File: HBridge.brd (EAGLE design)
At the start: 59.7 x 53.3 mm, 42 parts, among them IC1 74HC08D, IC2 A4954, J1 In 3/4, J2 Power, J3 In 1/2, J4 Output A, J5 Output B, J6 Digital_8_13, J7 Analog, J8 Digital_0_7

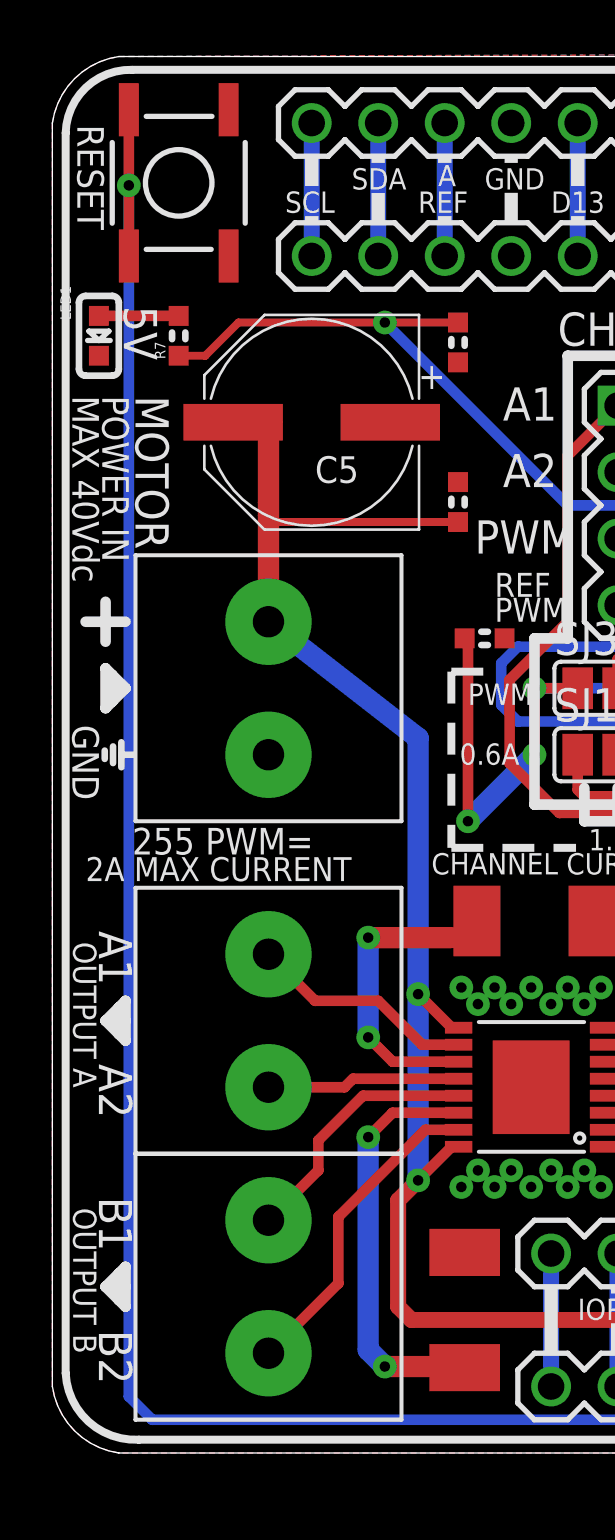
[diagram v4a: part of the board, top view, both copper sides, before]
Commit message: Replaced reset button with smaller 2-pin version
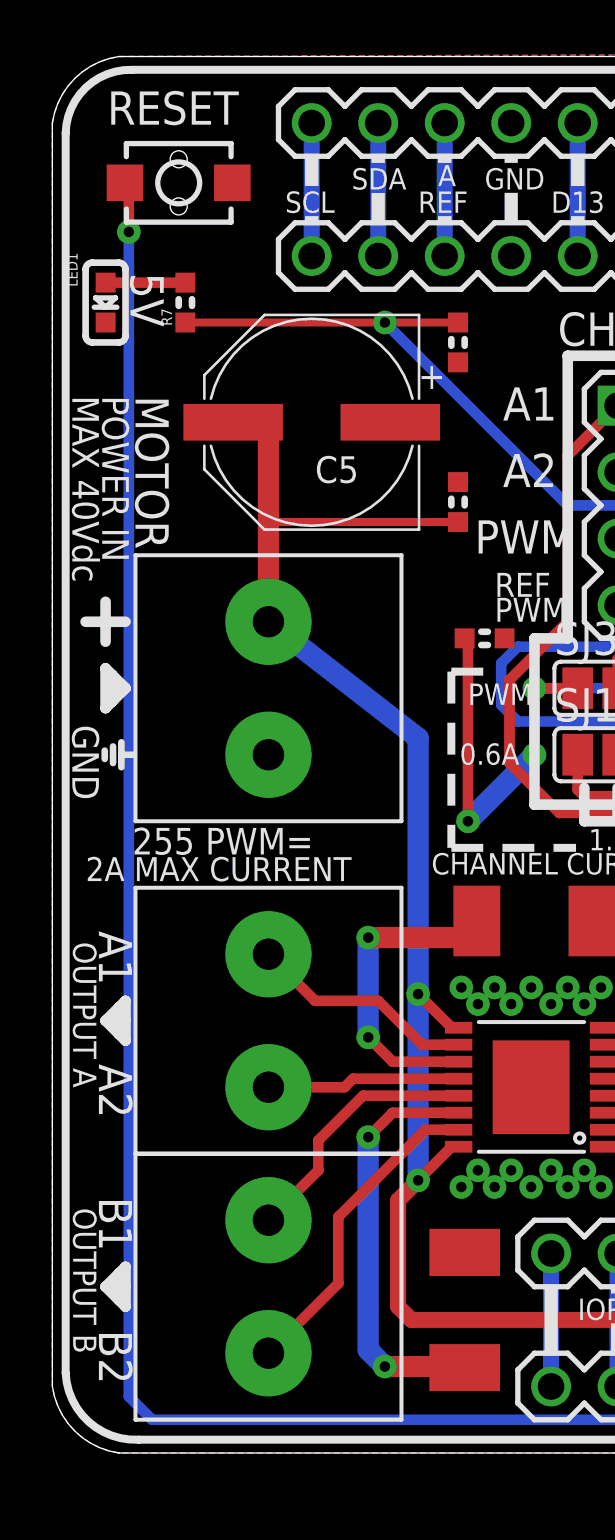
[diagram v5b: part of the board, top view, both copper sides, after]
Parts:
- S1: device freetronics:TACTILE_SWITCH_SMD -> freetronics-master-v1:TACTILE_SWITCH_SMD_2PIN_TINY
- moved R7 1.30 mm to (5.08, 43.9)
- moved LED1 1.30 mm to (2.03, 43.9)
- turned S1 to 0 degrees
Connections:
- net GND: no longer S1.1
- net RESET: now also S1.1; no longer S1.3, S1.4
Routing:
- net RESET: track 136.2 -> 130.8 mm
- net +5V: track 193.4 -> 192.6 mm
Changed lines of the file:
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@@
 <wire x1="28.09875" y1="27.78125" x2="28.09875" y2="27.305" width="0.3048" layer="21"/>
 <wire x1="28.09875" y1="27.305" x2="27.6225" y2="27.305" width="0.3048" layer="21"/>
-<text x="0.9525" y="50.7365" size="1.016" layer="21" ratio="15" rot="SR270">RESET</text>
-<text x="2.7305" y="43.815" size="1.27" layer="21" ratio="15" rot="SR270">5V</text>
+<text x="2.0955" y="50.7365" size="1.27" layer="21" ratio="15" rot="SR0">RESET</text>
+<text x="2.9845" y="45.085" size="1.27" layer="21" ratio="15" rot="SR270">5V</text>
 <text x="13.97" y="40.64" size="1.016" layer="21" ratio="15">+</text>
 <text x="1.778" y="19.939" size="1.27" layer="21" ratio="15" rot="SR270">A1</text>
@@
 <text x="26.9875" y="42.037" size="1.9304" layer="21" ratio="15">~</text>
 <text x="24.4475" y="42.037" size="1.9304" layer="21" ratio="15">~</text>
-<wire x1="2.286" y1="44.196" x2="1.27" y2="44.196" width="0.254" layer="21"/>
-<wire x1="1.27" y1="44.196" x2="1.016" y2="43.942" width="0.254" layer="21" curve="90"/>
-<wire x1="1.016" y1="43.942" x2="1.016" y2="41.402" width="0.254" layer="21"/>
-<wire x1="1.016" y1="41.402" x2="1.27" y2="41.148" width="0.254" layer="21" curve="90"/>
-<wire x1="1.27" y1="41.148" x2="2.286" y2="41.148" width="0.254" layer="21"/>
-<wire x1="2.286" y1="41.148" x2="2.54" y2="41.402" width="0.254" layer="21" curve="90"/>
-<wire x1="2.54" y1="41.402" x2="2.54" y2="43.942" width="0.254" layer="21"/>
-<wire x1="2.54" y1="43.942" x2="2.286" y2="44.196" width="0.254" layer="21" curve="90"/>
+<wire x1="2.54" y1="45.466" x2="1.524" y2="45.466" width="0.254" layer="21"/>
+<wire x1="1.524" y1="45.466" x2="1.27" y2="45.212" width="0.254" layer="21" curve="90"/>
+<wire x1="1.27" y1="45.212" x2="1.27" y2="42.672" width="0.254" layer="21"/>
+<wire x1="1.27" y1="42.672" x2="1.524" y2="42.418" width="0.254" layer="21" curve="90"/>
+<wire x1="1.524" y1="42.418" x2="2.54" y2="42.418" width="0.254" layer="21"/>
+<wire x1="2.54" y1="42.418" x2="2.794" y2="42.672" width="0.254" layer="21" curve="90"/>
+<wire x1="2.794" y1="42.672" x2="2.794" y2="45.212" width="0.254" layer="21"/>
+<wire x1="2.794" y1="45.212" x2="2.54" y2="45.466" width="0.254" layer="21" curve="90"/>
 <rectangle x1="21.336" y1="3.81" x2="21.844" y2="4.953" layer="22" rot="R180"/>
 <rectangle x1="21.336" y1="3.81" x2="21.844" y2="4.953" layer="21"/>
@@
 <element name="SL3" library="freetronics" package="1X08" value="Digital_0_7" x="54.61" y="45.72" locked="yes" smashed="yes" rot="R180"/>
 <element name="C8" library="freetronics" package="0603" value="100nF" x="15.494" y="42.418" smashed="yes" rot="R270"/>
-<element name="S1" library="freetronics" package="TACTILE_SWITCH_SMD" value="RESET" x="4.826" y="48.514" smashed="yes" rot="R270"/>
-<element name="LED1" library="freetronics" package="LED-0603" value="BLUE" x="1.778" y="42.672" smashed="yes" rot="R270">
-<attribute name="NAME" x="0.3048" y="44.577" size="0.4064" layer="25" rot="R270"/>
-<attribute name="VALUE" x="0.3048" y="43.942" size="0.4064" layer="27" rot="R270"/>
+<element name="LED1" library="freetronics" package="LED-0603" value="BLUE" x="2.032" y="43.942" smashed="yes" rot="R270">
+<attribute name="NAME" x="0.5588" y="45.847" size="0.4064" layer="25" rot="R270"/>
+<attribute name="VALUE" x="0.5588" y="45.212" size="0.4064" layer="27" rot="R270"/>
 </element>
-<element name="R7" library="freetronics" package="0603" value="2K2" x="4.826" y="42.672" smashed="yes" rot="R90">
-<attribute name="NAME" x="4.318" y="41.783" size="0.4064" layer="25" font="vector" rot="R90"/>
-<attribute name="VALUE" x="2.4892" y="41.656" size="0.4064" layer="27" font="vector" rot="R90"/>
+<element name="R7" library="freetronics" package="0603" value="2K2" x="5.08" y="43.942" smashed="yes" rot="R90">
+<attribute name="NAME" x="4.572" y="43.053" size="0.4064" layer="25" font="vector" rot="R90"/>
+<attribute name="VALUE" x="2.7432" y="42.926" size="0.4064" layer="27" font="vector" rot="R90"/>
 </element>
 <element name="IC2" library="freetronics-luke" package="TSSOP16-LP" value="A4954" x="18.288" y="13.97" smashed="yes" rot="R90"/>
@@
 <element name="SL5" library="freetronics" package="1X08" value="Digital_0_7" x="36.83" y="7.62" rot="R180"/>
 <element name="JP4" library="freetronics-master-v1" package="2X03" value="" x="56.02" y="27.89" rot="R270"/>
+<element name="S1" library="freetronics-master-v1" package="TACTILE_SWITCH_SMD_2PIN_TINY" value="RESET" x="4.826" y="48.514"/>
 </elements>
 <signals>
@@
 </signal>
 <signal name="RESET">
-<contactref element="S1" pad="3"/>
-<contactref element="S1" pad="4"/>
 <wire x1="22.86" y1="1.27" x2="3.81" y2="1.27" width="0.4064" layer="16"/>
 <contactref element="SL4" pad="6"/>
@@
 <wire x1="22.86" y1="1.27" x2="24.13" y2="2.54" width="0.4064" layer="16"/>
 <wire x1="24.13" y1="2.54" x2="24.13" y2="7.62" width="0.6096" layer="16"/>
-<via x="2.921" y="48.41875" extent="1-16" drill="0.4"/>
-<wire x1="2.921" y1="51.308" x2="2.921" y2="48.41875" width="0.4064" layer="1"/>
-<wire x1="2.921" y1="45.72" x2="2.921" y2="48.41875" width="0.4064" layer="1"/>
+<via x="2.921" y="46.64075" extent="1-16" drill="0.4"/>
 <wire x1="3.81" y1="1.27" x2="2.921" y2="2.159" width="0.4064" layer="16"/>
-<wire x1="2.921" y1="2.159" x2="2.921" y2="48.41875" width="0.4064" layer="16"/>
+<wire x1="2.921" y1="2.159" x2="2.921" y2="46.64075" width="0.4064" layer="16"/>
 <contactref element="JP4" pad="5"/>
 <wire x1="57.912" y1="22.86" x2="57.912" y2="5.842" width="0.254" layer="1"/>
@@
 <wire x1="54.864" y1="23.876" x2="54.864" y2="25.236" width="0.254" layer="1"/>
 <wire x1="54.864" y1="25.236" x2="54.75" y2="25.35" width="0.254" layer="1"/>
+<contactref element="S1" pad="1"/>
+<wire x1="2.921" y1="46.64075" x2="2.921" y2="48.514" width="0.4064" layer="1"/>
+<wire x1="2.921" y1="48.514" x2="2.776" y2="48.514" width="0.4064" layer="1"/>
 </signal>
 <signal name="AREF">
@@
 <contactref element="R7" pad="2"/>
 <contactref element="LED1" pad="A"/>
-<wire x1="1.778" y1="43.434" x2="4.826" y2="43.434" width="0.4064" layer="1"/>
+<wire x1="2.032" y1="44.704" x2="5.08" y2="44.704" width="0.4064" layer="1"/>
 </signal>
 <signal name="N$24">
@@
 <contactref element="J6" pad="7"/>
 <contactref element="C8" pad="2"/>
-<contactref element="S1" pad="2"/>
-<contactref element="S1" pad="1"/>
 <polygon width="0.4064" layer="16">
 <vertex x="0" y="50.8" curve="-73.740878"/>
@@
 <via x="20.955" y="17.78" extent="1-16" drill="0.4"/>
 <contactref element="JP4" pad="6"/>
+<contactref element="S1" pad="2"/>
 </signal>
 <signal name="N$192">
@@
 <wire x1="31.115" y1="15.875" x2="29.21" y2="17.78" width="0.6096" layer="16"/>
 <wire x1="12.7" y1="43.18" x2="15.494" y2="43.18" width="0.3048" layer="1"/>
-<wire x1="12.7" y1="43.18" x2="7.112" y2="43.18" width="0.3048" layer="1"/>
-<wire x1="5.842" y1="41.91" x2="4.826" y2="41.91" width="0.3048" layer="1"/>
-<wire x1="5.842" y1="41.91" x2="7.112" y2="43.18" width="0.3048" layer="1"/>
+<wire x1="12.7" y1="43.18" x2="5.08" y2="43.18" width="0.3048" layer="1"/>
 <contactref element="JP4" pad="2"/>
 <wire x1="58.166" y1="10.9855" x2="58.166" y2="22.86" width="0.8128" layer="16"/>

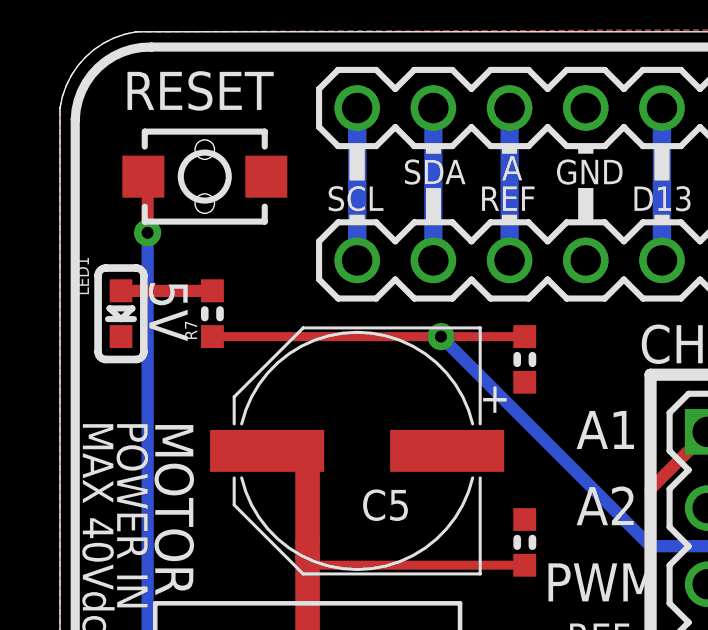
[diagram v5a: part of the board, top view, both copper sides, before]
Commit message: Improved position of pwr LED
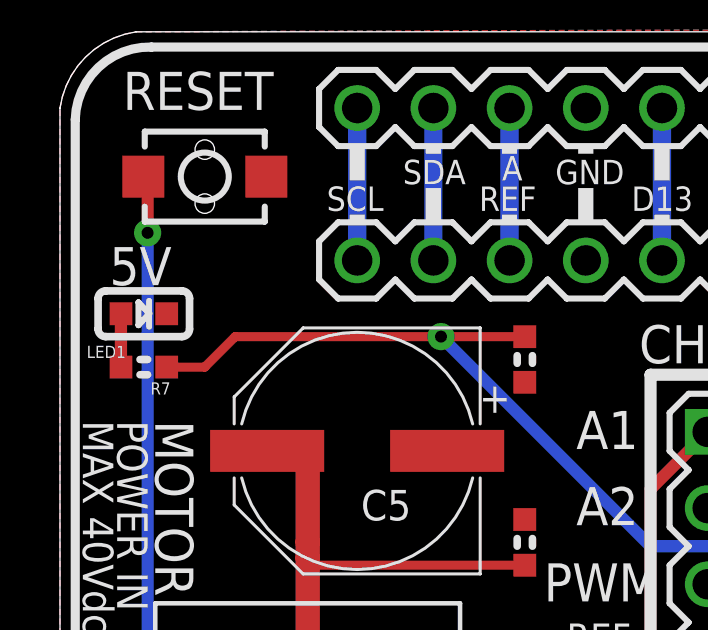
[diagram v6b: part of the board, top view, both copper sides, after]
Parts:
- moved R7 2.90 mm to (2.79, 42.2), turned to 180 degrees
- moved LED1 0.76 mm to (2.79, 43.9), turned to 0 degrees
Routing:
- net +5V: track 192.6 -> 194.5 mm
- net N$22: track 3.05 -> 1.78 mm
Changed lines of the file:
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@@
 <wire x1="28.09875" y1="27.305" x2="27.6225" y2="27.305" width="0.3048" layer="21"/>
 <text x="2.0955" y="50.7365" size="1.27" layer="21" ratio="15" rot="SR0">RESET</text>
-<text x="2.9845" y="45.085" size="1.27" layer="21" ratio="15" rot="SR270">5V</text>
+<text x="1.651" y="44.8945" size="1.27" layer="21" ratio="15" rot="SR0">5V</text>
 <text x="13.97" y="40.64" size="1.016" layer="21" ratio="15">+</text>
 <text x="1.778" y="19.939" size="1.27" layer="21" ratio="15" rot="SR270">A1</text>
@@
 <text x="26.9875" y="42.037" size="1.9304" layer="21" ratio="15">~</text>
 <text x="24.4475" y="42.037" size="1.9304" layer="21" ratio="15">~</text>
-<wire x1="2.54" y1="45.466" x2="1.524" y2="45.466" width="0.254" layer="21"/>
-<wire x1="1.524" y1="45.466" x2="1.27" y2="45.212" width="0.254" layer="21" curve="90"/>
-<wire x1="1.27" y1="45.212" x2="1.27" y2="42.672" width="0.254" layer="21"/>
-<wire x1="1.27" y1="42.672" x2="1.524" y2="42.418" width="0.254" layer="21" curve="90"/>
-<wire x1="1.524" y1="42.418" x2="2.54" y2="42.418" width="0.254" layer="21"/>
-<wire x1="2.54" y1="42.418" x2="2.794" y2="42.672" width="0.254" layer="21" curve="90"/>
-<wire x1="2.794" y1="42.672" x2="2.794" y2="45.212" width="0.254" layer="21"/>
-<wire x1="2.794" y1="45.212" x2="2.54" y2="45.466" width="0.254" layer="21" curve="90"/>
+<wire x1="1.27" y1="44.45" x2="1.27" y2="43.434" width="0.254" layer="21"/>
+<wire x1="1.27" y1="43.434" x2="1.524" y2="43.18" width="0.254" layer="21" curve="90"/>
+<wire x1="1.524" y1="43.18" x2="4.064" y2="43.18" width="0.254" layer="21"/>
+<wire x1="4.064" y1="43.18" x2="4.318" y2="43.434" width="0.254" layer="21" curve="90"/>
+<wire x1="4.318" y1="43.434" x2="4.318" y2="44.45" width="0.254" layer="21"/>
+<wire x1="4.318" y1="44.45" x2="4.064" y2="44.704" width="0.254" layer="21" curve="90"/>
+<wire x1="4.064" y1="44.704" x2="1.524" y2="44.704" width="0.254" layer="21"/>
+<wire x1="1.524" y1="44.704" x2="1.27" y2="44.45" width="0.254" layer="21" curve="90"/>
 <rectangle x1="21.336" y1="3.81" x2="21.844" y2="4.953" layer="22" rot="R180"/>
 <rectangle x1="21.336" y1="3.81" x2="21.844" y2="4.953" layer="21"/>
@@
 <element name="SL3" library="freetronics" package="1X08" value="Digital_0_7" x="54.61" y="45.72" locked="yes" smashed="yes" rot="R180"/>
 <element name="C8" library="freetronics" package="0603" value="100nF" x="15.494" y="42.418" smashed="yes" rot="R270"/>
-<element name="LED1" library="freetronics" package="LED-0603" value="BLUE" x="2.032" y="43.942" smashed="yes" rot="R270">
-<attribute name="NAME" x="0.5588" y="45.847" size="0.4064" layer="25" rot="R270"/>
-<attribute name="VALUE" x="0.5588" y="45.212" size="0.4064" layer="27" rot="R270"/>
+<element name="LED1" library="freetronics" package="LED-0603" value="BLUE" x="2.794" y="43.942" smashed="yes">
+<attribute name="NAME" x="0.889" y="42.4688" size="0.4064" layer="25"/>
+<attribute name="VALUE" x="1.524" y="42.4688" size="0.4064" layer="27"/>
 </element>
-<element name="R7" library="freetronics" package="0603" value="2K2" x="5.08" y="43.942" smashed="yes" rot="R90">
-<attribute name="NAME" x="4.572" y="43.053" size="0.4064" layer="25" font="vector" rot="R90"/>
-<attribute name="VALUE" x="2.7432" y="42.926" size="0.4064" layer="27" font="vector" rot="R90"/>
+<element name="R7" library="freetronics" package="0603" value="2K2" x="2.794" y="42.164" smashed="yes" rot="R180">
+<attribute name="NAME" x="3.683" y="41.656" size="0.4064" layer="25" font="vector" rot="R180"/>
+<attribute name="VALUE" x="3.81" y="39.8272" size="0.4064" layer="27" font="vector" rot="R180"/>
 </element>
 <element name="IC2" library="freetronics-luke" package="TSSOP16-LP" value="A4954" x="18.288" y="13.97" smashed="yes" rot="R90"/>
@@
 <contactref element="R7" pad="2"/>
 <contactref element="LED1" pad="A"/>
-<wire x1="2.032" y1="44.704" x2="5.08" y2="44.704" width="0.4064" layer="1"/>
+<wire x1="2.032" y1="43.942" x2="2.032" y2="42.164" width="0.4064" layer="1"/>
 </signal>
 <signal name="N$24">
@@
 <wire x1="31.115" y1="15.875" x2="29.21" y2="17.78" width="0.6096" layer="16"/>
 <wire x1="12.7" y1="43.18" x2="15.494" y2="43.18" width="0.3048" layer="1"/>
-<wire x1="12.7" y1="43.18" x2="5.08" y2="43.18" width="0.3048" layer="1"/>
+<wire x1="12.7" y1="43.18" x2="5.842" y2="43.18" width="0.3048" layer="1"/>
+<wire x1="5.842" y1="43.18" x2="4.826" y2="42.164" width="0.3048" layer="1"/>
+<wire x1="4.826" y1="42.164" x2="3.556" y2="42.164" width="0.3048" layer="1"/>
 <contactref element="JP4" pad="2"/>
 <wire x1="58.166" y1="10.9855" x2="58.166" y2="22.86" width="0.8128" layer="16"/>
